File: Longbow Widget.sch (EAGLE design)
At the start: 32 parts, among them J0 CONN_6SCREW_2.54, J1 CONN_6SCREW_2.54, J2 87832-14MALE, Q2 DMG3404, Q6 FDN360P, U1 TPS7A0533DBV

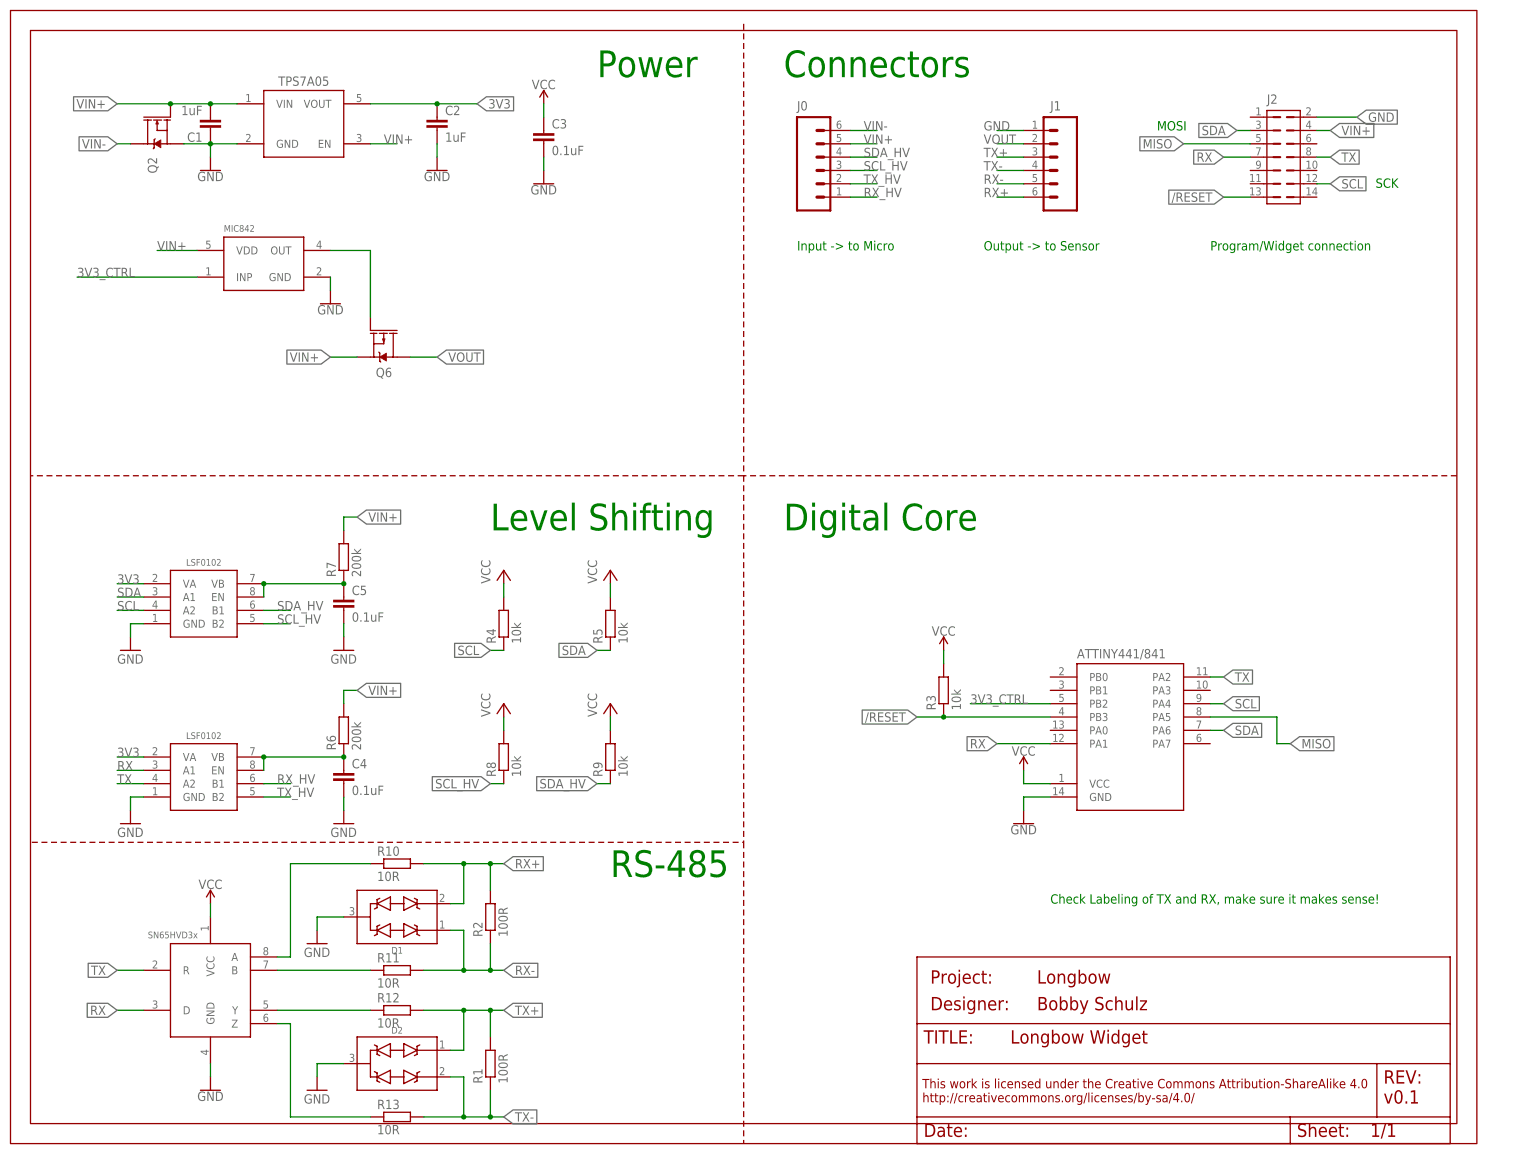
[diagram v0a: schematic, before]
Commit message: Updated Longbow Widget to use new Frames
Updated to used new frames without Creative Commons text (caused issues)
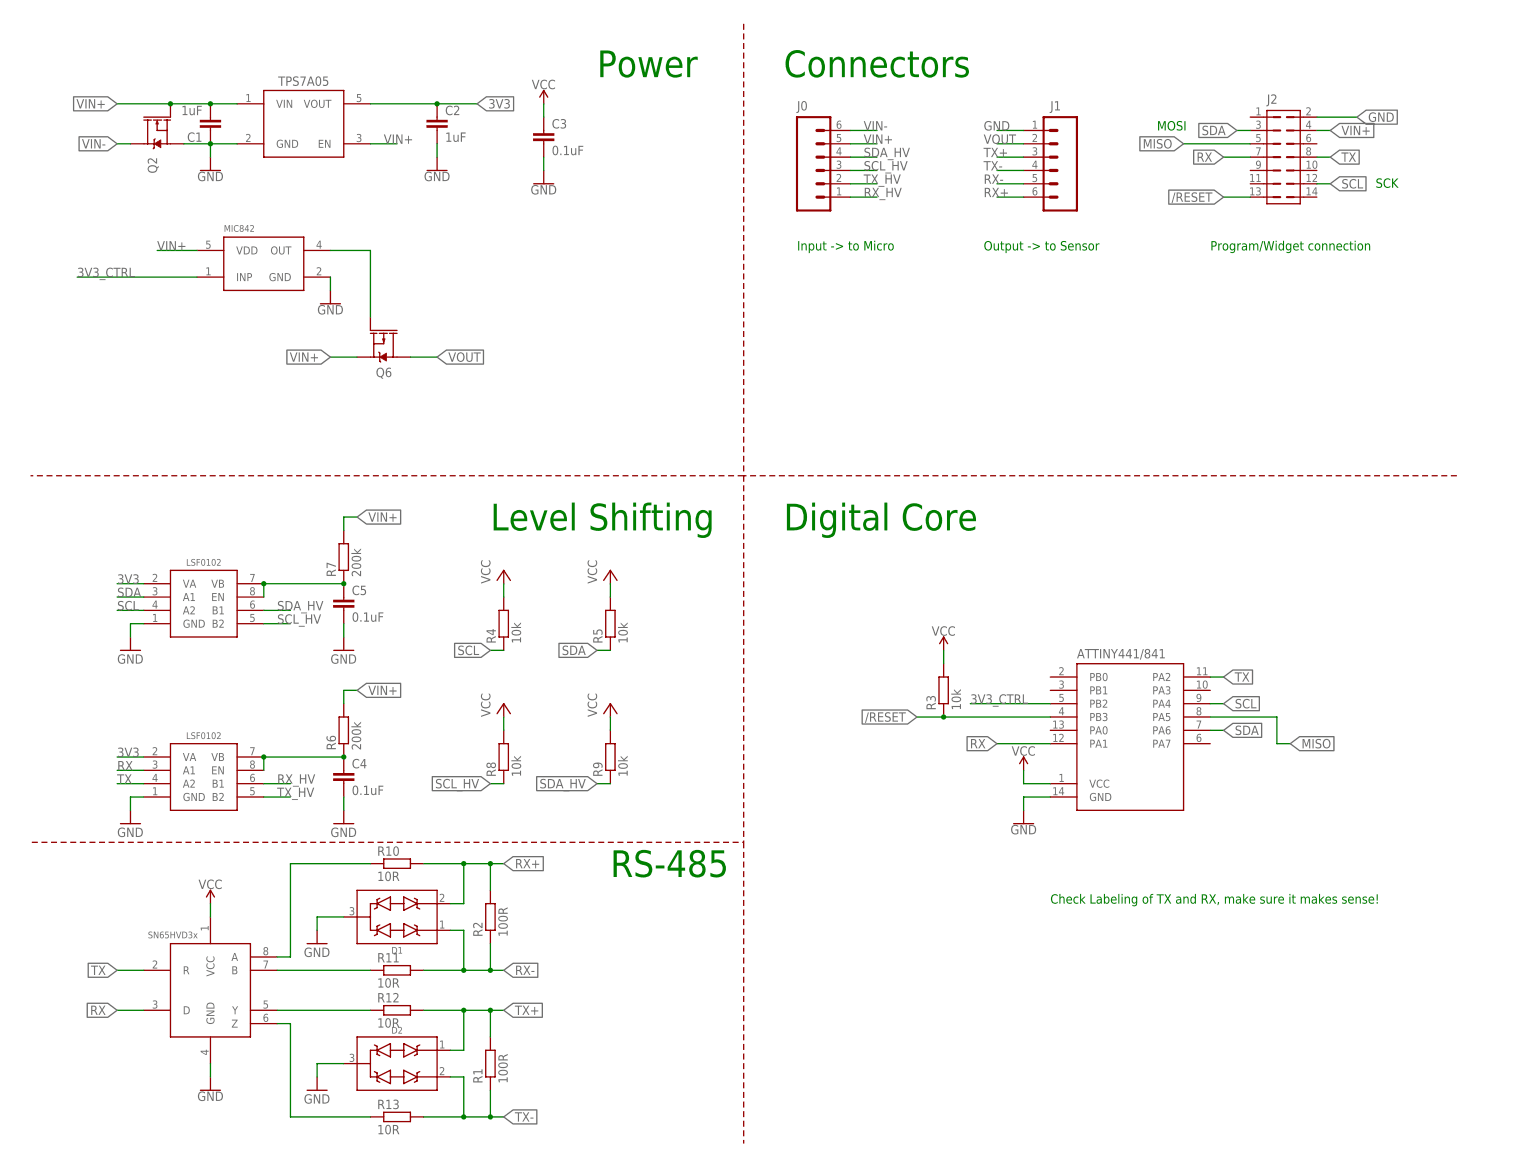
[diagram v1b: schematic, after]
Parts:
- removed FRAME1: (no value), bschulz:FRAME_A_L

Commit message: Updated Longbow Widget, v0.2 ready for review
Made changes to new level shifters, RS485 driver with output shutoff, replaced mosfet with load switch, converted MCU to QFN package. Ready for final review
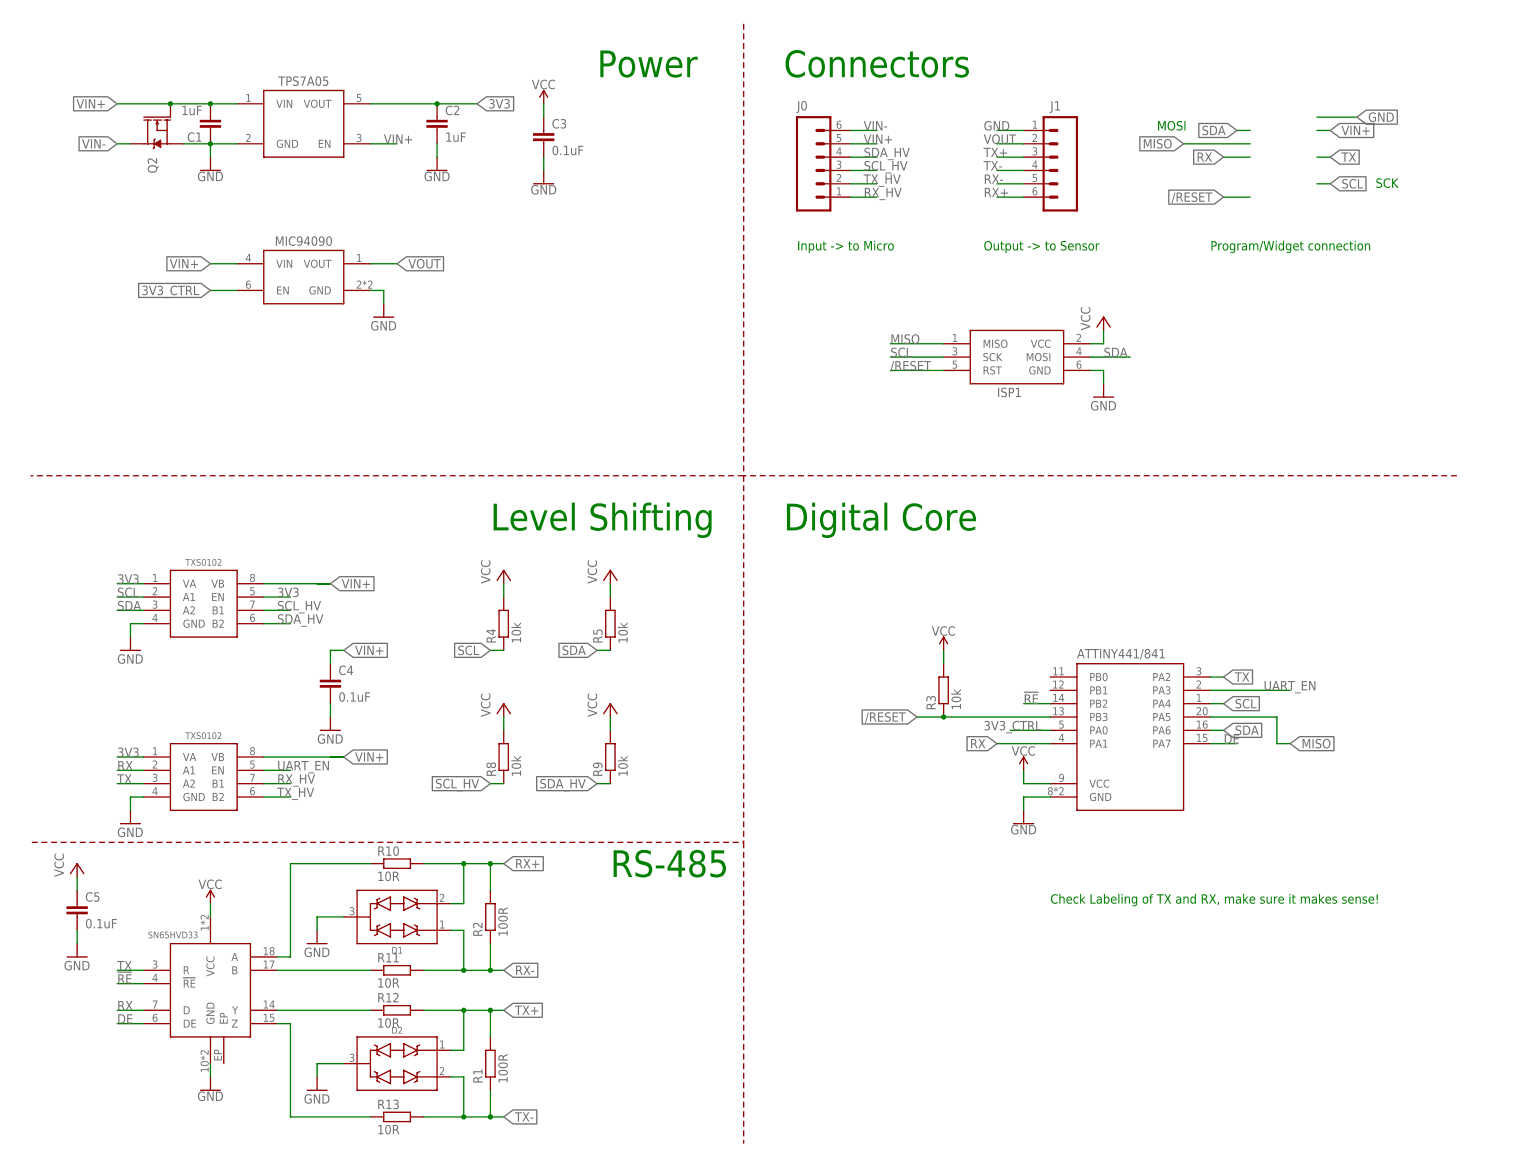
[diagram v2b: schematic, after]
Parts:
- removed J2: 87832-14MALE, bschulz:87832-14MALE
- removed Q6: FDN360P, bschulz:MOSFET_PCH-FDN360P
- removed R6, R7: 200k, bschulz_passives:R-EU_200KR0402
- removed U$11: MIC842H, bschulz:MIC842H
- added ISP1: AVRISP1.27MM, bschulz:AVRISP1.27MM
- added U2: SN65HVD33RHL, bschulz:SN65HVD33RHL
- U$1: value SN65HVD30 -> MIC94090C6; device bschulz:SN65HVD30 -> bschulz:MIC94090C6
- U$2: value ATTINY441/841841 -> ATTINY441/841VQFN; device bschulz:ATTINY441/841841 -> bschulz:ATTINY441/841VQFN
- U$3, U$6: value LSF0102DQE -> TXS0102DQM; device bschulz:LSF0102DQE -> bschulz:TXS0102DQM
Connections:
- removed net N$1: C5.1, R7.1, U$3.EN, U$3.VB
- removed net N$3: C4.1, R6.1, U$6.EN, U$6.VB
- removed net N$4: Q6.G, U$11.OUT
- new net !RE: U$2.PB2, U2.!RE
- new net DE: U$2.PA7, U2.DE
- new net UART_EN: U$2.PA3, U$6.EN
- net /RESET: now also ISP1.RST; no longer J2.13
- net 3V3: now also C5.1, ISP1.VCC, U$3.EN, U2.VCC; no longer U$1.VCC
- net 3V3_CTRL: now also U$1.EN, U$2.PA0; no longer U$11.INP, U$2.PB2
- net GND: now also ISP1.GND, U2.GND; no longer J2.2, U$11.GND
- net MISO: now also ISP1.MISO; no longer J2.5
- net N$2: now also U2.A; no longer U$1.A
- net N$5: now also U2.B; no longer U$1.B
- net N$6: now also U2.Y; no longer U$1.Y
- net N$7: now also U2.Z; no longer U$1.Z
- net RX: now also U2.D; no longer J2.7, U$1.D
- net SCL: now also ISP1.SCK, U$3.A1; no longer J2.12, U$3.A2
- net SCL_HV: now also U$3.B1; no longer U$3.B2
- net SDA: now also ISP1.MOSI, U$3.A2; no longer J2.3, U$3.A1
- net SDA_HV: now also U$3.B2; no longer U$3.B1
- net TX: now also U2.R; no longer J2.8, U$1.R
- net VIN+: now also C4.1, U$1.VIN, U$3.VB, U$6.VB; no longer J2.4, Q6.S, R6.2, R7.2, U$11.VDD
- net VOUT: now also U$1.VOUT; no longer Q6.D
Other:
- moved on the sheet: C4, C5

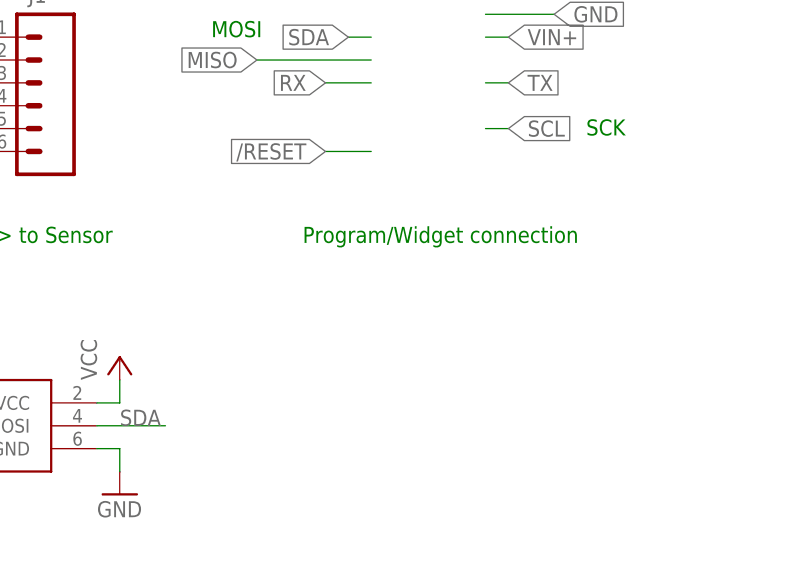
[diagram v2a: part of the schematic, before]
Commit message: Longbow Widget v0.2 sent to fab
Minor edits to silkscreen on longbow widget, v0.2 timeline, generated gerbers for Longbow Widget
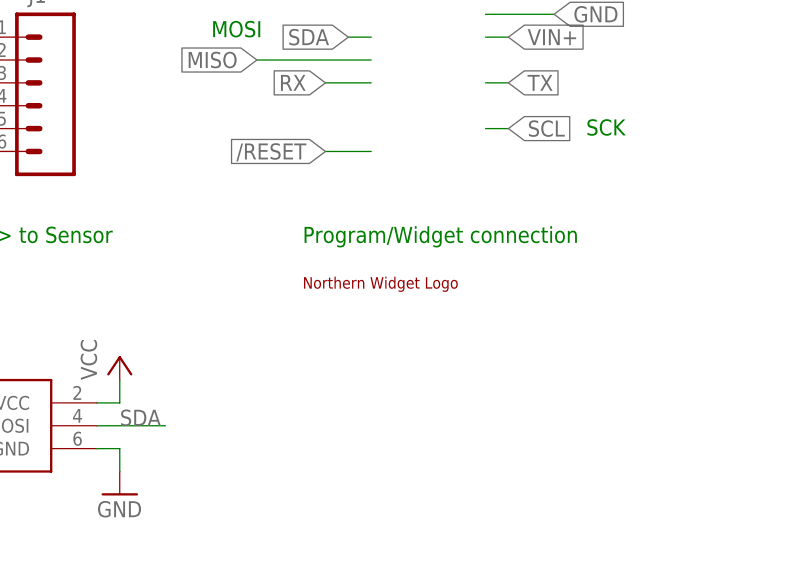
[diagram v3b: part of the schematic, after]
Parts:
- added U$4: NWLOGO_MED, awickert:NWLOGO_MED
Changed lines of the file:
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@@
 <part name="P+6" library="supply1" library_urn="urn:adsk.eagle:library:371" deviceset="VCC" device=""/>
 <part name="GND13" library="supply1" library_urn="urn:adsk.eagle:library:371" deviceset="GND" device=""/>
+<part name="U$4" library="awickert" deviceset="NWLOGO_MED" device=""/>
 </parts>
 <sheets>
@@
 <instance part="P+6" gate="VCC" x="12.7" y="53.34"/>
 <instance part="GND13" gate="1" x="12.7" y="35.56"/>
+<instance part="U$4" gate="G$1" x="236.22" y="165.1"/>
 </instances>
 <busses>
